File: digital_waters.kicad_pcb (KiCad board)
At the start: 4 copper layers, 188.5 x 82 mm, 118 parts, among them J1 pH_IN, J10 ESP_Only, J11 ESP32 [R], J12 SPI_EXPANSION, J13 I2C_EXPANSION, J14 Calibration_In, J16 ESP32 [L], J17 Atlas Surveyor, J18 EZO Carrier Board, J2 PT-100_TEMP_IN, J24 RPi Zero 2 W, J3 ORP_In, J4 Turbidity TSW-10, J5 SPARE, J8 SHARED, J9 RPi_Only, U1 MCP3208, U11 OPA2397DGKR, U13 TLV4387, U17 DHT20, U2 M24C02-FMN, U3 ESDA5V3SC5, U4 OPA2397DGKR, U5 OPA2397DGKR, U6 TPS22929D, U7 REF3040, U8 REF3025, U9 ESDA5V3SC5

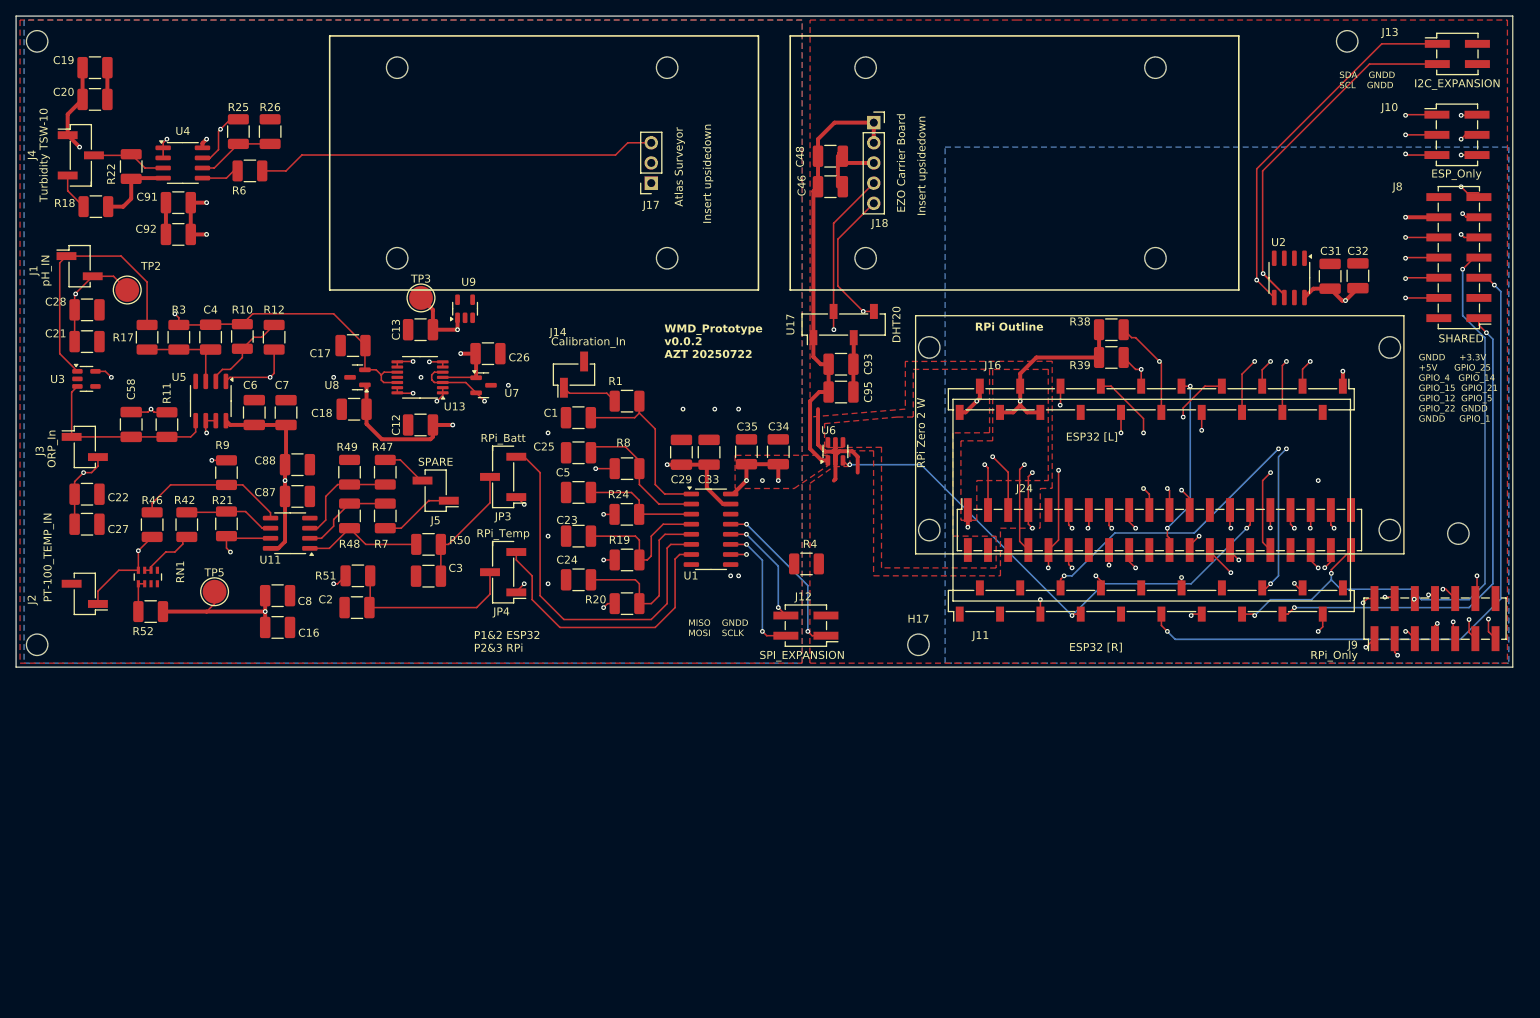
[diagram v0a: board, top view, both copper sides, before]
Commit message: Prototype v0.3.1 WIP Just a maintenance checkin. Many changes - Removed the Base Sensor schematic and put all sensors into SensorPrototype - Added a constant current LED driver for camera illumination - Added a 12V buck converter to the input in support of external power - Added a low-side current sense to the input - Added an LDO regulator to cleanup Buck output and to provide battery regulation - Added support for an internal battery + switchover / charge circuit. - Swapped headers for proper board connectors - Added an RS485 transceiver for external + modem communication - Added an additional temperature circuit in support of NTC probes - Incorporated the AS Dissolved Oxygen sensor into the main board - Added DC return path resistors to non-inverting amps - Fixed mixed power domain bug - Moved AS isolated carrier board to 3.3V rail and routed the shutdown pin to en/sh - Moved the DHT20 to the 3.3V rail - In the process of re-routing ADC channels.
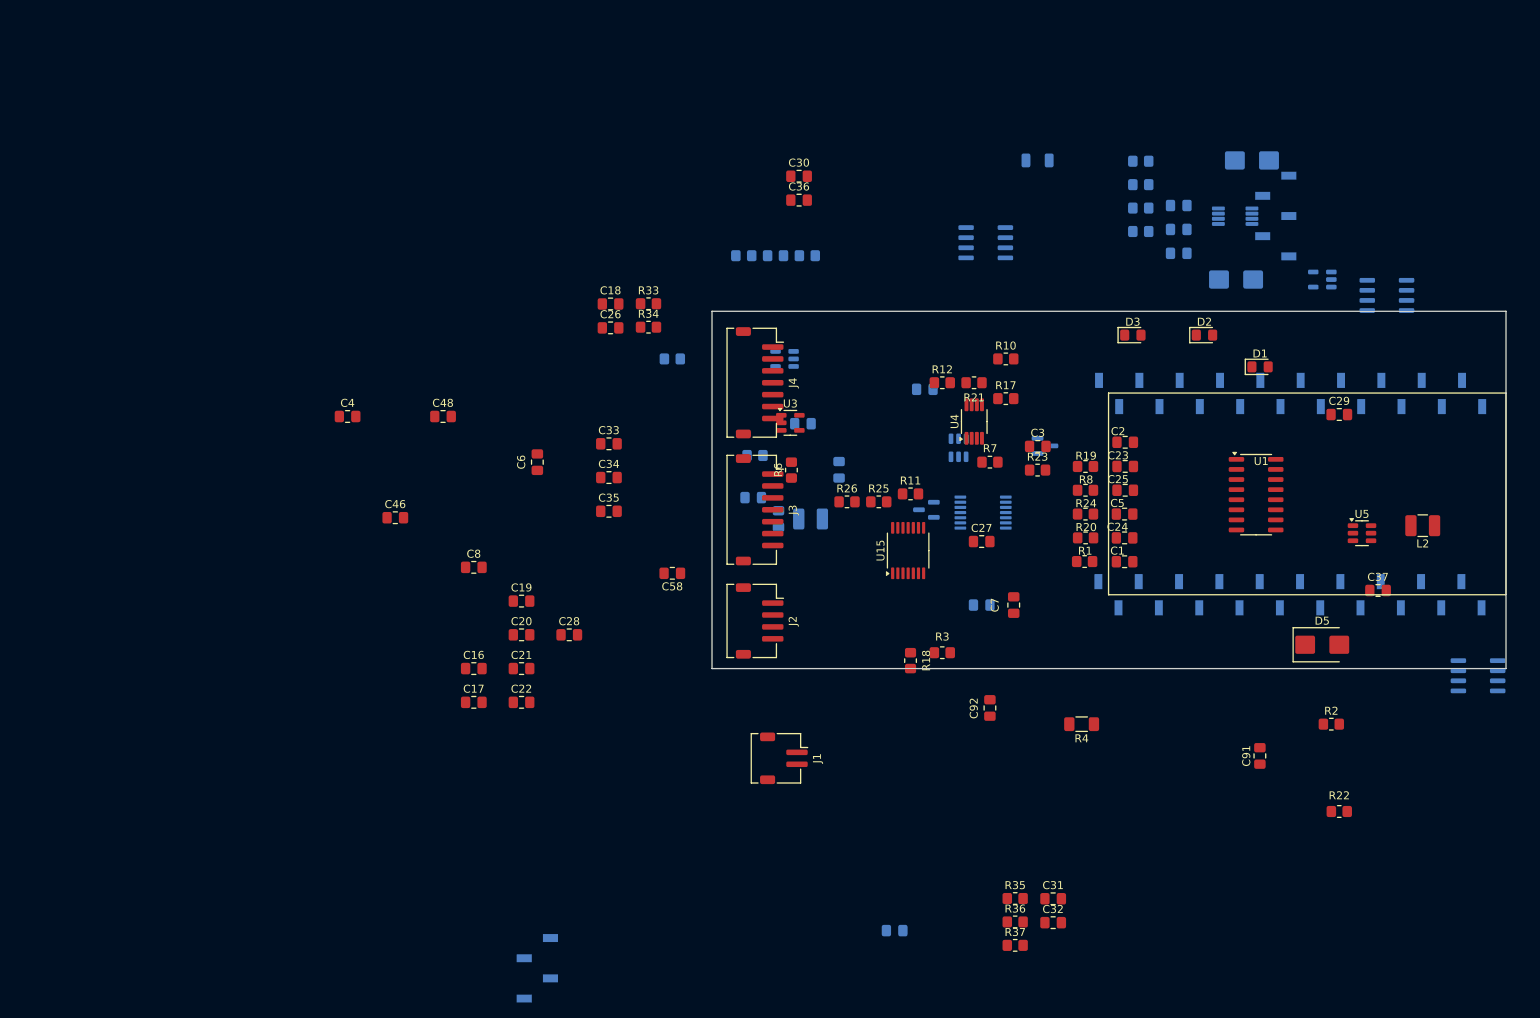
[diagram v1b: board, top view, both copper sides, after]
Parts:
- removed C87, C93: 0.1u, Capacitor_SMD:C_1210_3225Metric_Pad1.33x2.70mm_HandSolder
- removed C88, C95: 1u, Capacitor_SMD:C_1210_3225Metric_Pad1.33x2.70mm_HandSolder
- removed H1, H10, H11, H12, H13, H14, H15, H16, H17, H2, H3, H4, H5, H6, H7, H8, H9: MountingHole, MountingHole:MountingHole_2.7mm_M2.5_ISO14580
- removed J10: ESP_Only, Connector_PinHeader_2.54mm:PinHeader_2x03_P2.54mm_Vertical_SMD
- removed J12: SPI_EXPANSION, Connector_PinHeader_2.54mm:PinHeader_2x02_P2.54mm_Vertical_SMD
- removed J13: I2C_EXPANSION, Connector_PinHeader_2.54mm:PinHeader_2x02_P2.54mm_Vertical_SMD
- removed J14: Calibration_In, Connector_PinHeader_2.54mm:PinHeader_1x02_P2.54mm_Vertical_SMD_Pin1Left
- removed J17: Atlas Surveyor, Connector_PinSocket_2.54mm:PinSocket_1x03_P2.54mm_Vertical
- removed J24: RPi Zero 2 W, Connector_PinSocket_2.54mm:PinSocket_2x20_P2.54mm_Vertical_SMD
- removed J5: SPARE, Connector_PinHeader_2.54mm:PinHeader_1x02_P2.54mm_Vertical_SMD_Pin1Left
- removed J8: SHARED, Connector_PinHeader_2.54mm:PinHeader_2x07_P2.54mm_Vertical_SMD
- removed J9: RPi_Only, Connector_PinHeader_2.54mm:PinHeader_2x07_P2.54mm_Vertical_SMD
- removed JP3: RPi_Batt, Connector_PinHeader_2.54mm:PinHeader_1x03_P2.54mm_Vertical_SMD_Pin1Left
- removed JP4: RPi_Temp, Connector_PinHeader_2.54mm:PinHeader_1x03_P2.54mm_Vertical_SMD_Pin1Left
- removed R38, R39, R42, R46: 10k, Resistor_SMD:R_1210_3225Metric_Pad1.30x2.65mm_HandSolder
- removed R47: 10, Resistor_SMD:R_1210_3225Metric_Pad1.30x2.65mm_HandSolder
- removed R48, R49: 200, Resistor_SMD:R_1210_3225Metric_Pad1.30x2.65mm_HandSolder
- removed R50, R51, R52: 1k, Resistor_SMD:R_1210_3225Metric_Pad1.30x2.65mm_HandSolder
- removed RN1: 1k / 0.1%, Resistor_SMD:R_Array_Concave_4x0603
- removed TP2: +2.5V_REF, TestPoint:TestPoint_Pad_D3.0mm
- removed TP3: VSW, TestPoint:TestPoint_Pad_D3.0mm
- removed TP5: +4.096V_REF, TestPoint:TestPoint_Pad_D3.0mm
- removed U17: DHT20, Connector_PinSocket_2.54mm:PinSocket_1x04_P2.54mm_Vertical_SMD_Pin1Left
- added C10: 100nF, Capacitor_SMD:C_0805_2012Metric_Pad1.18x1.45mm_HandSolder, B.Cu at (151.4, 94.2)
- added C11: 22u, Capacitor_SMD:C_0805_2012Metric_Pad1.18x1.45mm_HandSolder, B.Cu at (148.4, 106.2)
- added C14: 22u, Capacitor_SMD:C_0805_2012Metric_Pad1.18x1.45mm_HandSolder, B.Cu at (145.2, 103.5)
- added C15: 10u, Capacitor_SMD:C_0805_2012Metric_Pad1.18x1.45mm_HandSolder, B.Cu at (166.8, 89.8)
- added C30: 0.47u, Capacitor_SMD:C_0805_2012Metric_Pad1.18x1.45mm_HandSolder, F.Cu at (151.0, 63.0)
- added C36: 0.47u, Capacitor_SMD:C_0805_2012Metric_Pad1.18x1.45mm_HandSolder, F.Cu at (151.0, 66.0)
- added C37: 0.47u, Capacitor_SMD:C_0805_2012Metric_Pad1.18x1.45mm_HandSolder, F.Cu at (223.9, 115.2)
- added C38: 1u, Capacitor_SMD:C_0805_2012Metric_Pad1.18x1.45mm_HandSolder, B.Cu at (198.8, 66.7)
- added C39: 0.1u, Capacitor_SMD:C_0805_2012Metric_Pad1.18x1.45mm_HandSolder, B.Cu at (198.8, 69.7)
- added C40: 1u, Capacitor_SMD:C_0805_2012Metric_Pad1.18x1.45mm_HandSolder, B.Cu at (198.8, 72.7)
- added C9: 10uF, Capacitor_SMD:C_0805_2012Metric_Pad1.18x1.45mm_HandSolder, B.Cu at (156.0, 100.0)
- added D1: LED, LED_SMD:LED_0805_2012Metric_Pad1.15x1.40mm_HandSolder, F.Cu at (209.0, 87.0)
- added D2: 5V Global, LED_SMD:LED_0805_2012Metric_Pad1.15x1.40mm_HandSolder, F.Cu at (202.0, 83.0)
- added D3: 5V Switched, LED_SMD:LED_0805_2012Metric_Pad1.15x1.40mm_HandSolder, F.Cu at (193.0, 83.0)
- added D4: B230, Diode_SMD:D_SMB, B.Cu at (206.0, 76.0)
- added D5: B230, Diode_SMD:D_SMB, F.Cu at (216.8, 122.0)
- added D6: B230, Diode_SMD:D_SMB, B.Cu at (208.0, 61.0)
- added L1: 3.3uH, Inductor_SMD:L_1210_3225Metric_Pad1.42x2.65mm_HandSolder, B.Cu at (152.4, 106.2)
- added L2: 22uH, Inductor_SMD:L_1210_3225Metric_Pad1.42x2.65mm_HandSolder, F.Cu at (229.5, 107.0)
- added R13: 470, Resistor_SMD:R_0805_2012Metric_Pad1.20x1.40mm_HandSolder, B.Cu at (148.0, 73.0)
- added R15: 62k / 1%, Resistor_SMD:R_0805_2012Metric_Pad1.20x1.40mm_HandSolder, B.Cu at (135.0, 86.0)
- added R16: 10k, Resistor_SMD:R_0805_2012Metric_Pad1.20x1.40mm_HandSolder, B.Cu at (145.4, 98.2)
- added R2: 100k, Resistor_SMD:R_0805_2012Metric_Pad1.20x1.40mm_HandSolder, F.Cu at (218.0, 132.0)
- added R23: 27k/1%, Resistor_SMD:R_0805_2012Metric_Pad1.20x1.40mm_HandSolder, F.Cu at (181.0, 100.0)
- added R28: 0.1 / 1% / 0.5W / Metal Film, Resistor_SMD:R_1206_3216Metric, B.Cu at (181.0, 61.0)
- added R29: 10k / 1%, Resistor_SMD:R_0805_2012Metric_Pad1.20x1.40mm_HandSolder, B.Cu at (194.0, 61.1)
- added R30: 10k / 1%, Resistor_SMD:R_0805_2012Metric_Pad1.20x1.40mm_HandSolder, B.Cu at (194.0, 64.0)
- added R31: 100k / 1%, Resistor_SMD:R_0805_2012Metric_Pad1.20x1.40mm_HandSolder, B.Cu at (194.0, 67.0)
- added R32: 100k / 1%, Resistor_SMD:R_0805_2012Metric_Pad1.20x1.40mm_HandSolder, B.Cu at (194.0, 70.0)
- added R33: 4.7k, Resistor_SMD:R_0805_2012Metric_Pad1.20x1.40mm_HandSolder, F.Cu at (132.0, 79.0)
- added R34: 4.7k, Resistor_SMD:R_0805_2012Metric_Pad1.20x1.40mm_HandSolder, F.Cu at (132.0, 82.0)
- added R35: 27k/1%, Resistor_SMD:R_0805_2012Metric_Pad1.20x1.40mm_HandSolder, F.Cu at (178.2, 154.0)
- added R36: 1k, Resistor_SMD:R_0805_2012Metric_Pad1.20x1.40mm_HandSolder, F.Cu at (178.2, 156.9)
- added R37: 1k, Resistor_SMD:R_0805_2012Metric_Pad1.20x1.40mm_HandSolder, F.Cu at (178.2, 159.9)
- added R5: 2k, Resistor_SMD:R_0805_2012Metric_Pad1.20x1.40mm_HandSolder, B.Cu at (152.0, 73.0)
- added U10: ST485E, Package_SO:SOIC-8_3.9x4.9mm_P1.27mm, B.Cu at (225.0, 78.0)
- added U12: DHT20, Connector_PinSocket_2.54mm:PinSocket_1x04_P2.54mm_Vertical_SMD_Pin1Left, B.Cu at (118.0, 162.8)
- added U14: MCP1727-5002xSN, Package_SO:SOIC-8_3.9x4.9mm_P1.27mm, B.Cu at (174.5, 71.4)
- added U15: TLV4387, Package_SO:TSSOP-14_4.4x5mm_P0.65mm, F.Cu at (164.7, 110.1)
- added U16: AP63200WU, Package_TO_SOT_SMD:TSOT-23-6, B.Cu at (149.1, 86.0)
- C1: value 800n -> 0.1u; footprint Capacitor_SMD:C_1210_3225Metric_Pad1.33x2.70mm_HandSolder -> Capacitor_SMD:C_0805_2012Metric_Pad1.18x1.45mm_HandSolder
- C12, C13: footprint Capacitor_SMD:C_1210_3225Metric_Pad1.33x2.70mm_HandSolder -> Capacitor_SMD:C_0805_2012Metric_Pad1.18x1.45mm_HandSolder; moved to B.Cu
- C16, C19, C21, C22: value 10u -> 0.1u; footprint Capacitor_SMD:C_1210_3225Metric_Pad1.33x2.70mm_HandSolder -> Capacitor_SMD:C_0805_2012Metric_Pad1.18x1.45mm_HandSolder
- C17: value 10u -> 800n; footprint Capacitor_SMD:C_1210_3225Metric_Pad1.33x2.70mm_HandSolder -> Capacitor_SMD:C_0805_2012Metric_Pad1.18x1.45mm_HandSolder
- C18, C2, C20, C23, C24, C25, C27, C28, C29, C3, C31, C32, C33, C34, C35, C4, C46, C48, C5, C58, C6, C7, C8, C91, C92: footprint Capacitor_SMD:C_1210_3225Metric_Pad1.33x2.70mm_HandSolder -> Capacitor_SMD:C_0805_2012Metric_Pad1.18x1.45mm_HandSolder
- C26: value 1u -> 0.1u; footprint Capacitor_SMD:C_1210_3225Metric_Pad1.33x2.70mm_HandSolder -> Capacitor_SMD:C_0805_2012Metric_Pad1.18x1.45mm_HandSolder
- J1: value pH_IN -> Conn_01x02; footprint Connector_PinHeader_2.54mm:PinHeader_1x02_P2.54mm_Vertical_SMD_Pin1Left -> Connector_JST:JST_ZH_S2B-ZR-SM4A-TF_1x02-1MP_P1.50mm_Horizontal
- J11, J16, U13, U2, U6, U7, U8, U9: moved to B.Cu
- J18: footprint Connector_PinSocket_2.54mm:PinSocket_1x05_P2.54mm_Vertical -> Connector_PinSocket_2.54mm:PinSocket_1x05_P2.54mm_Vertical_SMD_Pin1Left; moved to B.Cu
- J2: value PT-100_TEMP_IN -> Conn_01x04; footprint Connector_PinHeader_2.54mm:PinHeader_1x02_P2.54mm_Vertical_SMD_Pin1Left -> Connector_JST:JST_ZH_S4B-ZR-SM4A-TF_1x04-1MP_P1.50mm_Horizontal
- J3: value ORP_In -> Conn_01x07; footprint Connector_PinHeader_2.54mm:PinHeader_1x02_P2.54mm_Vertical_SMD_Pin1Left -> Connector_JST:JST_ZH_S7B-ZR-SM4A-TF_1x07-1MP_P1.50mm_Horizontal
- J4: value Turbidity TSW-10 -> Conn_01x07; footprint Connector_PinHeader_2.54mm:PinHeader_1x03_P2.54mm_Vertical_SMD_Pin1Left -> Connector_JST:JST_ZH_S7B-ZR-SM4A-TF_1x07-1MP_P1.50mm_Horizontal
- R1, R11, R19, R20, R24, R3, R8: footprint Resistor_SMD:R_1210_3225Metric_Pad1.30x2.65mm_HandSolder -> Resistor_SMD:R_0805_2012Metric_Pad1.20x1.40mm_HandSolder
- R10: value 10k -> 1k / 1%; footprint Resistor_SMD:R_1210_3225Metric_Pad1.30x2.65mm_HandSolder -> Resistor_SMD:R_0805_2012Metric_Pad1.20x1.40mm_HandSolder
- R12: value 5k -> 27k/1%; footprint Resistor_SMD:R_1210_3225Metric_Pad1.30x2.65mm_HandSolder -> Resistor_SMD:R_0805_2012Metric_Pad1.20x1.40mm_HandSolder
- R17: value 3.3k -> 10k/1%; footprint Resistor_SMD:R_1210_3225Metric_Pad1.30x2.65mm_HandSolder -> Resistor_SMD:R_0805_2012Metric_Pad1.20x1.40mm_HandSolder
- R18: value 470 -> 470/1%; footprint Resistor_SMD:R_1210_3225Metric_Pad1.30x2.65mm_HandSolder -> Resistor_SMD:R_0805_2012Metric_Pad1.20x1.40mm_HandSolder
- R21: value 100k -> 10k/1%; footprint Resistor_SMD:R_1210_3225Metric_Pad1.30x2.65mm_HandSolder -> Resistor_SMD:R_0805_2012Metric_Pad1.20x1.40mm_HandSolder
- R22: value 4.7k -> 4.7k/1%; footprint Resistor_SMD:R_1210_3225Metric_Pad1.30x2.65mm_HandSolder -> Resistor_SMD:R_0805_2012Metric_Pad1.20x1.40mm_HandSolder
- R25: value 114k -> 96k / 1%; footprint Resistor_SMD:R_1210_3225Metric_Pad1.30x2.65mm_HandSolder -> Resistor_SMD:R_0805_2012Metric_Pad1.20x1.40mm_HandSolder
- R26: value 1k -> 100 / 1%; footprint Resistor_SMD:R_1210_3225Metric_Pad1.30x2.65mm_HandSolder -> Resistor_SMD:R_0805_2012Metric_Pad1.20x1.40mm_HandSolder
- R4: footprint Resistor_SMD:R_1210_3225Metric_Pad1.30x2.65mm_HandSolder -> Resistor_SMD:R_1206_3216Metric_Pad1.30x1.75mm_HandSolder
- R6: value 990 -> 100; footprint Resistor_SMD:R_1210_3225Metric_Pad1.30x2.65mm_HandSolder -> Resistor_SMD:R_0805_2012Metric_Pad1.20x1.40mm_HandSolder
- R7: value 10 -> 1k / 1%; footprint Resistor_SMD:R_1210_3225Metric_Pad1.30x2.65mm_HandSolder -> Resistor_SMD:R_0805_2012Metric_Pad1.20x1.40mm_HandSolder
- R9: value 100k -> 470; footprint Resistor_SMD:R_1210_3225Metric_Pad1.30x2.65mm_HandSolder -> Resistor_SMD:R_0805_2012Metric_Pad1.20x1.40mm_HandSolder; moved to B.Cu
- U11: value OPA2397DGKR -> OPA197xDGK; footprint Package_SO:SOIC-8_3.9x4.9mm_P1.27mm -> Package_SO:VSSOP-8_3x3mm_P0.65mm; moved to B.Cu
- U4: value OPA2397DGKR -> TLV2387DGKR; footprint Package_SO:SOIC-8_3.9x4.9mm_P1.27mm -> Package_SO:VSSOP-8_3x3mm_P0.65mm
- U5: value OPA2397DGKR -> DIO5661ST6; footprint Package_SO:SOIC-8_3.9x4.9mm_P1.27mm -> Package_TO_SOT_SMD:SOT-23-6
- moved R22 172.5 mm to (219.0, 143.0), turned to 0 degrees
- moved C91 153.0 mm to (209.0, 136.0), turned to 90 degrees
- moved U5 145.9 mm to (221.9, 108.0), turned to 0 degrees
- moved U11 125.5 mm to (205.9, 68.0)
- moved C92 118.3 mm to (175.0, 130.0), turned to 90 degrees
- moved R18 117.5 mm to (165.0, 124.0), turned to -90 degrees
- moved C27 112.7 mm to (174.0, 109.0)
- moved R17 108.4 mm to (177.0, 91.0), turned to 0 degrees
- moved J1 108.2 mm to (149.1, 136.3), turned to -90 degrees
- moved U9 108.0 mm to (216.9, 76.0), turned to 180 degrees
- moved U4 104.9 mm to (173.0, 93.9), turned to 90 degrees
- moved R3 104.0 mm to (169.0, 123.0), turned to 0 degrees
- moved C2 99.0 mm to (192.0, 96.5), turned to 0 degrees
- moved C13 96.4 mm to (163.0, 158.0)
- moved R10 96.2 mm to (177.0, 86.0), turned to 0 degrees
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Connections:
- net /Base_Sensor/+4.096_REF_BUF_A renamed /Power/+4.096_REF_BUF_A
- C1 pad 1: /ADC.CAL -> +3.3V
- C1 pad 2: GNDA -> GNDD
- C12 pad 1: +VSW -> /Power/+5V_SW
- C12 pad 2: GNDA -> /Power/ANALOG_GND
- C13 pad 1: +VSW -> /Power/+5V_SW
- C13 pad 2: GNDA -> /Power/ANALOG_GND
- C16 pad 2: GNDA -> /Power/ANALOG_GND
- C17 pad 1: /Base_Sensor/+2.5V_REF -> /Sensor Module Prototype/ADC_CAL
- C17 pad 2: GNDA -> /Sensor Module Prototype/ANALOG_GND
- C18 pad 1: +VSW -> +3.3V
- C18 pad 2: GNDA -> GNDD
- C19 pad 2: GNDA -> /Power/ANALOG_GND
- C2 pad 1: Net-(JP4-C) -> /Sensor Module Prototype/ADC_TEMP_NTC_10k
- C2 pad 2: GNDA -> /Sensor Module Prototype/ANALOG_GND
- C20 pad 2: GNDA -> /Power/ANALOG_GND
- C21 pad 2: GNDA -> /Power/ANALOG_GND
- C22 pad 2: GNDA -> /Power/ANALOG_GND
- C23 pad 1: /ADC.PH -> /Sensor Module Prototype/ADC_PH
- C23 pad 2: GNDA -> /Sensor Module Prototype/ANALOG_GND
- C24 pad 1: /ADC.ORP -> /Sensor Module Prototype/ADC_ORP
- C24 pad 2: GNDA -> /Sensor Module Prototype/ANALOG_GND
- C25 pad 1: /ADC.TURB -> /Sensor Module Prototype/ADC_TURB
- C25 pad 2: GNDA -> /Sensor Module Prototype/ANALOG_GND
- C26 pad 1: +VSW -> +3.3V
- C26 pad 2: GNDA -> GNDD
- C27 pad 2: GNDA -> /Power/ANALOG_GND
- C28 pad 2: GNDA -> /Power/ANALOG_GND
- C29 pad 1: VDDA -> +5V
- C29 pad 2: GNDA -> GNDD
- C3 pad 1: Net-(JP3-C) -> /Sensor Module Prototype/ADC_TEMP_PT_1000
- C3 pad 2: GNDA -> /Sensor Module Prototype/ANALOG_GND
- C31 pad 1: +3.3V -> /Sensor Module Prototype/VDD
- C31 pad 2: GNDD -> /Sensor Module Prototype/ANALOG_GND
- C32 pad 1: +3.3V -> /Sensor Module Prototype/VDD
- C32 pad 2: GNDD -> /Sensor Module Prototype/ANALOG_GND
- C33 pad 1: VDDA -> unconnected-(C33-Pad1)
- C33 pad 2: GNDA -> Net-(C33-Pad2)
- C34 pad 1: +VSW -> Net-(C34-Pad1)
- C34 pad 2: GNDA -> Net-(C33-Pad2)
- C35 pad 1: +VSW -> Net-(C34-Pad1)
- C35 pad 2: GNDA -> Net-(C33-Pad2)
- C4 pad 1: Net-(U5A-+) -> /Sensor Module Prototype/INPUT_pH+
- C4 pad 2: /Base_Sensor/+2.5V_REF -> /Sensor Module Prototype/ANALOG_GND
- C46 pad 1: +VSW -> +3.3V
- C46 pad 2: GNDD -> /Sensor Module Prototype/DIGITAL_GND
- C48 pad 1: +VSW -> +3.3V
- C48 pad 2: GNDD -> /Sensor Module Prototype/DIGITAL_GND
- C5 pad 1: /ADC.DO -> /Sensor Module Prototype/ADC_DO
- C5 pad 2: GNDA -> /Sensor Module Prototype/ANALOG_GND
- C58 pad 1: Net-(J3-In) -> /Sensor Module Prototype/INPUT_ORP+
- C58 pad 2: /Base_Sensor/+2.5V_REF -> /Sensor Module Prototype/ANALOG_GND
- C6 pad 1: +VSW -> /Sensor Module Prototype/VDD
- C6 pad 2: GNDA -> /Sensor Module Prototype/ANALOG_GND
- C7 pad 1: +VSW -> /Sensor Module Prototype/VDD
- C7 pad 2: GNDA -> /Sensor Module Prototype/ANALOG_GND
- C8 pad 2: GNDA -> /Power/ANALOG_GND
- C91 pad 1: +VSW -> /Sensor Module Prototype/VDD
- C91 pad 2: GNDA -> /Sensor Module Prototype/ANALOG_GND
- C92 pad 1: +VSW -> /Sensor Module Prototype/VDD
- C92 pad 2: GNDA -> /Sensor Module Prototype/ANALOG_GND
- J1 pad 1: Net-(J1-In) -> unconnected-(J1-Pin_1-Pad1)
- J1 pad 2: /Power/+2.5V_REF_BUF_A -> unconnected-(J1-Pin_2-Pad2)
- J11 pad 16: /Micocontroller/GPIO_3_ESP -> /Micocontroller/GPIO_3_U0RXD
- J11 pad 17: /Micocontroller/GPIO_1 -> /Micocontroller/GPIO_1_U0TXD
- J11 pad 6: /Micocontroller/GPIO_2_ESP -> /Micocontroller/GPIO_2
- J11 pad 7: /EN/~{SH_0} -> /Micocontroller/EN/~{SH_0}
- J16 pad 3: /Micocontroller/GPIO_36_ESP -> /Micocontroller/GPIO_36
- J16 pad 4: /Micocontroller/GPIO_39_ESP -> /Micocontroller/GPIO_39
- J16 pad 5: /Micocontroller/GPIO_34_ESP -> /Micocontroller/GPIO_34
- J16 pad 6: /Micocontroller/GPIO_35_ESP -> /Micocontroller/GPIO_35
- J16 pad 7: /Base_Sensor/VBATT_BUF -> /Micocontroller/GPIO_32_COM_DE/RE*
- J16 pad 8: /Base_Sensor/TEMP_SENSE_BUF -> /Micocontroller/GPIO_33
- J18 pad 1: +VSW -> +3.3V
- J18 pad 2: +VSW -> /Sensor Module Prototype/EN/~{SH_0}
- J18 pad 3: GNDD -> /Sensor Module Prototype/DIGITAL_GND
- J18 pad 4: /I2C_SDA -> /Sensor Module Prototype/I2C_SDA
- J18 pad 5: /I2C_SCL -> /Sensor Module Prototype/I2C_SCL
- J2 pad 1: Net-(J2-In) -> unconnected-(J2-Pin_1-Pad1)
- J2 pad 2: GNDA -> unconnected-(J2-Pin_2-Pad2)
- J3 pad 1: Net-(J3-In) -> unconnected-(J3-Pin_1-Pad1)
- J3 pad 2: /Power/+2.5V_REF_BUF_B -> unconnected-(J3-Pin_2-Pad2)
- J4 pad 1: /Power/+4.096_REF_BUF_B -> unconnected-(J4-Pin_1-Pad1)
- J4 pad 2: Net-(J4-Pin_2) -> unconnected-(J4-Pin_2-Pad2)
- J4 pad 3: Net-(J4-Pin_3) -> unconnected-(J4-Pin_3-Pad3)
- R1 pad 1: Net-(J14-Pin_1) -> unconnected-(R1-Pad1)
- R1 pad 2: /ADC.CAL -> /Sensor Module Prototype/ADC_CAL
- R10 pad 1: /Base_Sensor/+2.5V_REF -> /Sensor Module Prototype/ANALOG_GND
- R10 pad 2: Net-(U5A--) -> /Sensor Module Prototype/INPUT_PT1000-
- R11 pad 1: /Base_Sensor/+2.5V_REF -> /Sensor Module Prototype/ANALOG_GND
- R11 pad 2: Net-(J3-In) -> /Sensor Module Prototype/INPUT_ORP+
- R12 pad 1: Net-(U5A--) -> /Base_Sensor/ANALOG_GND
- R17 pad 1: Net-(J1-In) -> Net-(U4B-+)
- R17 pad 2: Net-(U5A-+) -> /Sensor Module Prototype/INPUT_NTC10K
- R18 pad 1: GNDA -> /Sensor Module Prototype/ANALOG_GND
- R18 pad 2: Net-(J4-Pin_3) -> /Sensor Module Prototype/INPUT_TURB_V-
- R19 pad 1: Net-(R12-Pad2) -> Net-(U15B--)
- R19 pad 2: /ADC.PH -> /Sensor Module Prototype/ADC_PH
- R20 pad 1: Net-(U5B--) -> Net-(U15C--)
- R20 pad 2: /ADC.ORP -> /Sensor Module Prototype/ADC_ORP
- R21 pad 1: Net-(U11B--) -> Net-(U4B--)
- R21 pad 2: Net-(R21-Pad2) -> /Sensor Module Prototype/INPUT_PT1000-
- R22 pad 1: GNDA -> /Sensor Module Prototype/ANALOG_GND
- R22 pad 2: Net-(J4-Pin_2) -> /Sensor Module Prototype/INPUT_TURB_SIG
- R24 pad 2: /ADC.DO -> /Sensor Module Prototype/ADC_DO
- R25 pad 1: Net-(U4B--) -> Net-(U15D--)
- R26 pad 1: GNDA -> /Sensor Module Prototype/ANALOG_GND
- R26 pad 2: Net-(U4B--) -> Net-(U15D--)
- R3 pad 1: /Base_Sensor/+2.5V_REF -> /Sensor Module Prototype/ANALOG_GND
- R3 pad 2: Net-(U5A-+) -> /Sensor Module Prototype/INPUT_pH+
- R4 pad 1: GNDD -> /Power/V_SENSE_+
- R4 pad 2: GNDA -> /Power/ANALOG_GND
- R6 pad 1: Net-(J17-Pin_3) -> /Sensor Module Prototype/INPUT_DO
- R6 pad 2: Net-(U4B-+) -> Net-(U15D-+)
- R7 pad 1: Net-(J5-Pin_1) -> /Sensor Module Prototype/INPUT_NTC10K
- R7 pad 2: Net-(U11A--) -> /Sensor Module Prototype/+4.096_REF_BUF_A
- R8 pad 1: Net-(U4A--) -> Net-(U15A--)
- R8 pad 2: /ADC.TURB -> /Sensor Module Prototype/ADC_TURB
- R9 pad 1: /Base_Sensor/+2.5V_REF -> /Power/+5V_IN
- R9 pad 2: Net-(U11B-+) -> Net-(D2-A)
- U1 pad 1: /ADC.CAL -> unconnected-(U1-CH0-Pad1)
- U1 pad 10: /SPI_CS0 -> unconnected-(U1-~{CS}/SHDN-Pad10)
- U1 pad 11: /SPI_MOSI -> unconnected-(U1-Din-Pad11)
- U1 pad 15: VDDA -> unconnected-(U1-Vref-Pad15)
- U1 pad 16: +VSW -> unconnected-(U1-Vdd-Pad16)
- U1 pad 2: /ADC.TURB -> unconnected-(U1-CH1-Pad2)
- U1 pad 3: /ADC.DO -> unconnected-(U1-CH2-Pad3)
- U1 pad 4: /ADC.PH -> unconnected-(U1-CH3-Pad4)
- U1 pad 5: /ADC.ORP -> unconnected-(U1-CH4-Pad5)
- U1 pad 6: /ADC.VBATT -> unconnected-(U1-CH5-Pad6)
- U1 pad 7: /ADC.TEMP -> unconnected-(U1-CH6-Pad7)
- U11 pad 1: Net-(R48-Pad2) -> unconnected-(U11-NC-Pad1)
- U11 pad 2: Net-(U11A--) -> Net-(U11--)
- U11 pad 4: GNDA -> /Power/DIG_PRE_GND
- U11 pad 5: Net-(U11B-+) -> unconnected-(U11-NC-Pad5)
- U11 pad 6: Net-(U11B--) -> /Power/ADC_ISENSE
- U11 pad 7: Net-(R21-Pad2) -> /Power/DIG_PRE_PWR
- U11 pad 8: +VSW -> unconnected-(U11-NC-Pad8)
- U13 pad 10: /Base_Sensor/+2.5V_REF -> Net-(U13C-+)
- U13 pad 11: GNDA -> /Power/ANALOG_GND
- U13 pad 12: /Base_Sensor/+2.5V_REF -> Net-(U13C-+)
- U13 pad 3: VDDA -> Net-(U13A-+)
- U13 pad 4: +VSW -> /Power/+5V_SW
- U13 pad 5: VDDA -> Net-(U13A-+)
- U3 pad 1: Net-(J1-In) -> /INPUT_OUTPUT_RS485_A
- U3 pad 2: GNDA -> /Sensor Module Prototype/ANALOG_GND
- U3 pad 3: Net-(J3-In) -> /INPUT_OUTPUT_RS485_B
- U3 pad 4: unconnected-(U3-Pad4) -> (no net)
- U3 pad 5: Net-(J2-In) -> /Sensor Module Prototype/INPUT_NTC10K
- U4 pad 3: Net-(J4-Pin_2) -> /Sensor Module Prototype/INPUT_NTC10K
- U4 pad 4: GNDA -> /Sensor Module Prototype/ANALOG_GND
- U4 pad 7: Net-(R24-Pad1) -> Net-(R23-Pad2)
- U4 pad 8: +VSW -> /Sensor Module Prototype/VDD
- U5 pad 1: Net-(R12-Pad2) -> Net-(D5-A)
- U5 pad 2: Net-(U5A--) -> GNDD
- U5 pad 3: Net-(U5A-+) -> /Micocontroller/OUTPUT_ILLUMINATOR-
- U5 pad 4: GNDA -> /Micocontroller/EN/~{SH_0}
- U5 pad 5: Net-(J3-In) -> unconnected-(U5-Pad5)
- U5 pad 6: Net-(U5B--) -> +5V
- U6 pad 1: +VSW -> /Power/+5V_SW
- U6 pad 2: GNDD -> /Power/V_SENSE_+
- U6 pad 3: /EN/~{SH_0} -> /Power/EN/~{SH}
- U6 pad 4: +5V -> /Power/+5V_IN
- U6 pad 5: GNDD -> /Power/V_SENSE_+
- U6 pad 6: +5V -> /Power/+5V_IN
- U7 pad 1: +VSW -> /Power/+5V_SW
- U7 pad 2: VDDA -> Net-(U13A-+)
- U7 pad 3: GNDA -> /Power/ANALOG_GND
- U8 pad 1: +VSW -> /Power/+5V_SW
- U8 pad 2: /Base_Sensor/+2.5V_REF -> Net-(U13C-+)
- U8 pad 3: GNDA -> /Power/ANALOG_GND
- U9 pad 1: +VSW -> (no net)
- U9 pad 2: GNDA -> /Power/DIG_PRE_GND
- U9 pad 3: unconnected-(U9-Pad3) -> (no net)
- U9 pad 4: unconnected-(U9-Pad4) -> /Power/INPUT_12V+
- U9 pad 5: unconnected-(U9-Pad5) -> (no net)
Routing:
- net /I2C_SDA: track 176.2 -> 0.00 mm, vias 4 -> 0
- net /I2C_SCL: track 165.6 -> 0.00 mm, vias 4 -> 0
- net +VSW: track 137.4 -> 0.00 mm, vias 10 -> 0
- net /SPI_MOSI: track 111.8 -> 0.00 mm, vias 4 -> 0
- net /Base_Sensor/TEMP_SENSE_BUF: track 102.0 -> 0.00 mm, vias 2 -> 0
- net /Micocontroller/GPIO_14: track 97.8 -> 0.00 mm, vias 3 -> 0
- net /Micocontroller/GPIO_2_ESP: track 96.5 -> 0.00 mm, vias 3 -> 0
- net /Base_Sensor/VBATT_BUF: track 96.1 -> 0.00 mm, vias 2 -> 0
- net /SPI_SCLK: track 94.0 -> 0.00 mm, vias 4 -> 0
- net /SPI_CS0: track 91.7 -> 0.00 mm, vias 3 -> 0
- net /SPI_MISO: track 91.6 -> 0.00 mm, vias 4 -> 0
- net /Micocontroller/GPIO_4: track 91.3 -> 0.00 mm, vias 4 -> 0
- net /Micocontroller/GPIO_5: track 89.2 -> 0.00 mm, vias 2 -> 0
- net /Micocontroller/GPIO_15: track 84.8 -> 0.00 mm, vias 4 -> 0
- net /Micocontroller/GPIO_21: track 82.6 -> 0.00 mm, vias 3 -> 0
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- removed copper zone on B.Cu, net +3.3V
- removed copper zone on F.Cu, net +3.3V
- removed copper zone on F.Cu, net +5V
- removed copper zone on F.Cu, net +VSW
- removed copper zone on In1.Cu, net +VSW
- removed copper zone on B.Cu, net GNDA
- removed copper zone on F.Cu, net GNDA
- removed copper zone on F.Cu, net GNDD
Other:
- board size 188.5 x 82 mm -> 100 x 45 mm
- board text removed: "GNDD +3.3V +5V GPIO_25 GPIO_4 GPIO_14 GPIO_15 GPIO_21 GPIO_12 GPIO_5 GPIO_22 GNDD GNDD GPIO_1"
- board text removed: "Insert upsidedown"
- board text removed: "MISO GNDD MOSI SCLK"
- board text removed: "P1&2 ESP32 P2&3 RPi"
- board text removed: "RPi Outline"
- board text removed: "SDA GNDD SCL GNDD"
- board text removed: "WMD_Prototype v0.0.2 AZT 20250722"
